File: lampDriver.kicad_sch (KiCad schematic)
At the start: 69 parts, among them IC8 1ED44175N01BXTSA1, Q2 BC847, Q4 BC807, T4 IMBG120R181M2HXTMA1, U1 OPA2356AIDGKR, U3 LM2901

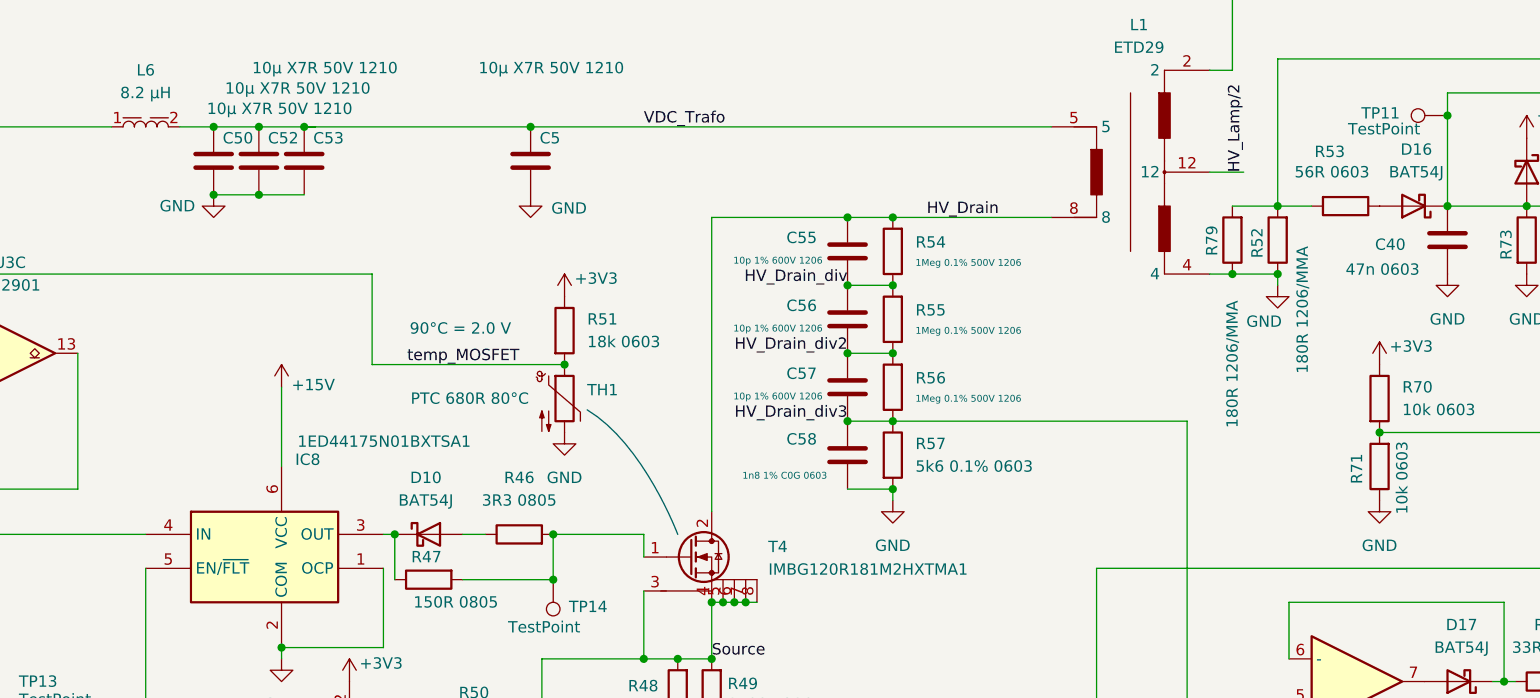
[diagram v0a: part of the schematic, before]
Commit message: prototyp V2 with bug fixes
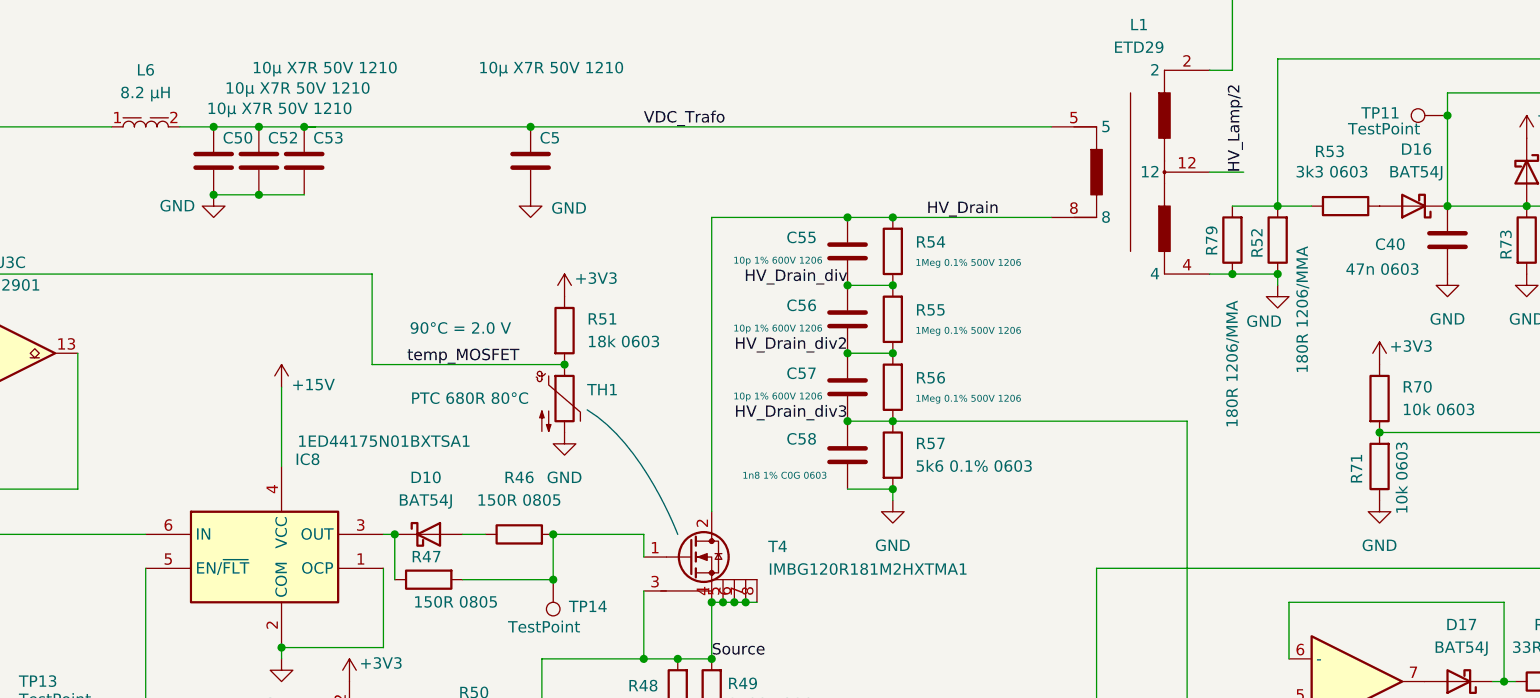
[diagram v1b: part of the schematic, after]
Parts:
- IC8: footprint SOT95P280X145-6N -> Hansmann_Gatetreiber:SOT95P280X145-5N
- R46: value 3R3 0805 -> 150R 0805
- R53: value 56R 0603 -> 3k3 0603
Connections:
- net +15V: now also IC8.4 (VCC); no longer IC8.6 (VCC)
- net at C49.1, R44.2: now also IC8.6 (IN); no longer IC8.4 (IN)
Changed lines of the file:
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@@
 			)
 		)
-		(property "Footprint" "SOT95P280X145-6N"
+		(property "Footprint" "Hansmann_Gatetreiber:SOT95P280X145-5N"
 			(at 95.25 176.2 0)
 			(effects
@@
 			)
 		)
-		(property "Value" "3R3 0805"
+		(property "Value" "150R 0805"
 			(at 105.41 80.01 90)
 			(effects
@@
 			)
 		)
-		(property "Value" "56R 0603"
+		(property "Value" "3k3 0603"
 			(at 196.596 43.18 90)
 			(effects

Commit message: prototyp V2 with fixed gate driver, test points missing
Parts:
- IC8: footprint Hansmann_Gatetreiber:SOT95P280X145-5N -> Package_TO_SOT_SMD:SOT-23-6
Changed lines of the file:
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@@
 			)
 		)
-		(property "Footprint" "Hansmann_Gatetreiber:SOT95P280X145-5N"
+		(property "Footprint" "Package_TO_SOT_SMD:SOT-23-6"
 			(at 95.25 176.2 0)
 			(effects

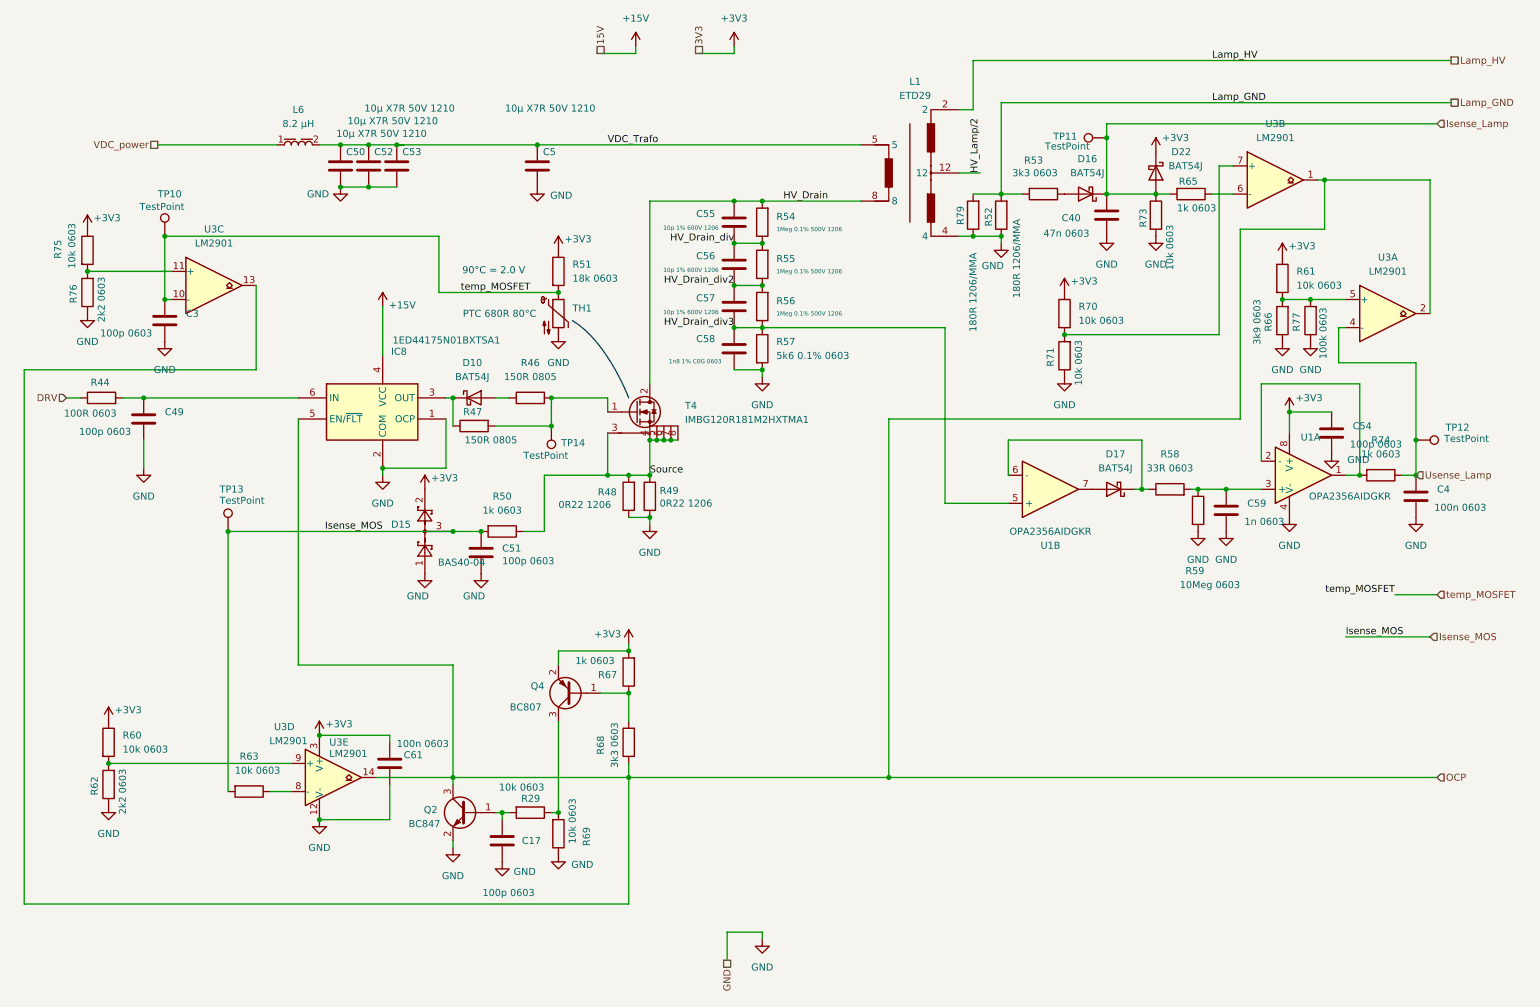
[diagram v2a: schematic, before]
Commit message: prototyp V2 with fixed gate driver, test points placed
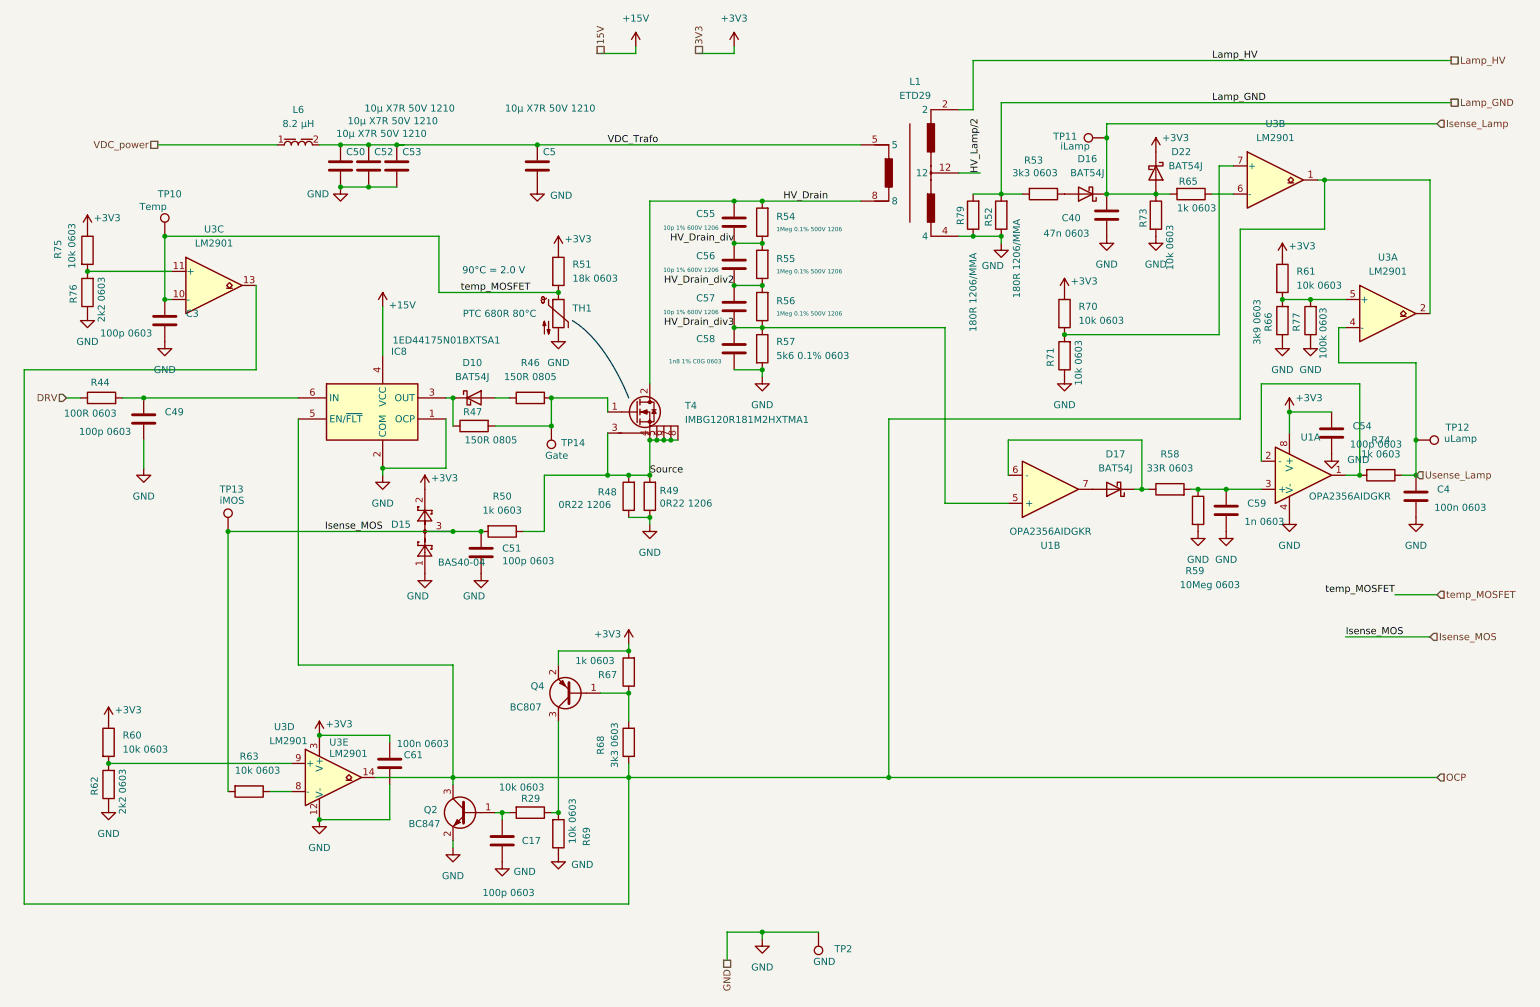
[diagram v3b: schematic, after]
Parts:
- added TP2: GND, TestPoint:TestPoint_THTPad_2.0x2.0mm_Drill1.0mm, symbol Connector:TestPoint
- TP10: value TestPoint -> Temp
- TP11: value TestPoint -> iLamp
- TP12: value TestPoint -> uLamp
- TP13: value TestPoint -> iMOS
- TP14: value TestPoint -> Gate
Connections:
- net GND: now also TP2.1
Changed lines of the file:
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@@
 	)
 	(junction
+		(at 147.32 180.34)
+		(diameter 0)
+		(color 0 0 0 0)
+	)
+	(junction
 		(at 242.57 86.36)
 		(diameter 0)
@@
 	(wire
 		(pts
+			(xy 147.32 180.34) (xy 157.48 180.34)
+		)
+		(stroke
+			(width 0)
+			(type default)
+		)
+	)
+	(wire
+		(pts
 			(xy 119.38 83.82) (xy 119.38 86.36)
 		)
@@
 			)
 		)
-		(property "Value" "TestPoint"
+		(property "Value" "Gate"
 			(at 112.268 94.234 0)
 			(effects
@@
 			)
 		)
-		(property "Value" "TestPoint"
+		(property "Value" "iLamp"
 			(at 206.502 38.354 90)
 			(effects
@@
 			)
 		)
-		(property "Value" "TestPoint"
+		(property "Value" "iMOS"
 			(at 49.276 102.362 0)
 			(effects
@@
 			)
 		)
-		(property "Value" "TestPoint"
+		(property "Value" "Temp"
 			(at 34.798 49.276 0)
 			(effects
@@
 	)
 	(symbol
+		(lib_id "Connector:TestPoint")
+		(at 157.48 180.34 180)
+		(unit 1)
+		(exclude_from_sim no)
+		(in_bom yes)
+		(on_board yes)
+		(dnp no)
+		(property "Reference" "TP2"
+			(at 163.576 183.388 0)
+			(effects
+				(font
+					(size 1.27 1.27)
+				)
+				(justify left)
+			)
+		)
+		(property "Value" "GND"
+			(at 160.528 185.674 0)
+			(effects
+				(font
+					(size 1.27 1.27)
+				)
+				(justify left)
+			)
+		)
+		(property "Footprint" "TestPoint:TestPoint_THTPad_2.0x2.0mm_Drill1.0mm"
+			(at 152.4 180.34 0)
+			(effects
+				(font
+					(size 1.27 1.27)
+				)
+				(hide yes)
+			)
+		)
+		(property "Datasheet" ""
+			(at 152.4 180.34 0)
+			(effects
+				(font
+					(size 1.27 1.27)
+				)
+				(hide yes)
+			)
+		)
+		(property "Description" "test point"
+			(at 157.48 180.34 0)
+			(effects
+				(font
+					(size 1.27 1.27)
+				)
+				(hide yes)
+			)
+		)
+		(pin "1"
+		)
+		(instances
+			(project "OSLUV"
+				(path "/c6e900e0-9399-44f0-8089-9dd7b8ffe54c/9b3070c3-43e0-4d43-9da1-9bc1bd2d6fb9/8926c1e3-dcc6-4ec7-96ae-5bdb4f87d364"
+					(reference "TP2")
+					(unit 1)
+				)
+			)
+		)
+	)
+	(symbol
 		(lib_id "Device:R")
 		(at 105.41 83.82 90)
@@
 			)
 		)
-		(property "Value" "TestPoint"
+		(property "Value" "uLamp"
 			(at 270.51 91.186 90)
 			(effects
